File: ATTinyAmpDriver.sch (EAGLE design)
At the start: 34 parts, among them Q1 SI2301CDS, Q2 BC846, U1 SPX5205M5-L-3-3, U2 ATTINY5-TSHR, U3 MCP6L2-X_SN, X2 INPUT

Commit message: Board Complete
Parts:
- removed X2: INPUT, con-phoenix-254:MPT3
- added U$1: CON_TAILLIGHT, Combined:CON_TAILLIGHT
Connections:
- net +14V: now also U$1.L1; no longer X2-1.1
- net GND: now also U$1.H2, U$1.L2; no longer X2-2.1
- net N$1: now also U$1.H1; no longer X2-3.1
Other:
- moved on the sheet: D1, R6, R7
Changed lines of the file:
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@@
 <attribute name="DIGIKEY_COST" value=".60"/>
 </part>
-<part name="X2" library="con-phoenix-254" deviceset="MPT3" device="" value="INPUT"/>
 <part name="SUPPLY1" library="supply2" deviceset="+14V" device=""/>
 <part name="SUPPLY2" library="supply2" deviceset="GND" device=""/>
@@
 <part name="LED4" library="Combined" deviceset="LUXEON_REBEL" device="CREE_XP-E"/>
 <part name="SUPPLY20" library="supply2" deviceset="GND" device=""/>
+<part name="U$1" library="Combined" deviceset="CON_TAILLIGHT" device=""/>
 </parts>
 <sheets>
@@
 <attribute name="DIGIKEY_COST" x="66.04" y="180.34" size="1.778" layer="96" display="off"/>
 </instance>
-<instance part="X2" gate="-1" x="81.28" y="132.08" rot="MR0"/>
-<instance part="X2" gate="-2" x="81.28" y="121.92" rot="MR0"/>
-<instance part="X2" gate="-3" x="81.28" y="127" rot="MR0"/>
-<instance part="SUPPLY1" gate="G$1" x="91.44" y="139.7"/>
-<instance part="SUPPLY2" gate="GND" x="91.44" y="114.3"/>
+<instance part="SUPPLY1" gate="G$1" x="91.44" y="144.78"/>
+<instance part="SUPPLY2" gate="GND" x="91.44" y="109.22"/>
 <instance part="SUPPLY3" gate="G$1" x="96.52" y="195.58"/>
 <instance part="C3" gate="G$1" x="91.44" y="172.72">
@@
 </instance>
 <instance part="SUPPLY9" gate="G$1" x="38.1" y="195.58"/>
-<instance part="R6" gate="G$1" x="106.68" y="127" rot="R180">
-<attribute name="DIGIKEY" x="106.68" y="127" size="1.778" layer="96" rot="R180" display="off"/>
-<attribute name="DIGIKEY_COST" x="106.68" y="127" size="1.778" layer="96" rot="R180" display="off"/>
-</instance>
-<instance part="R7" gate="G$1" x="114.3" y="119.38" rot="R270">
-<attribute name="DIGIKEY" x="114.3" y="119.38" size="1.778" layer="96" rot="R270" display="off"/>
-<attribute name="DIGIKEY_COST" x="114.3" y="119.38" size="1.778" layer="96" rot="R270" display="off"/>
-</instance>
-<instance part="SUPPLY10" gate="GND" x="114.3" y="109.22"/>
+<instance part="R6" gate="G$1" x="106.68" y="132.08" rot="R180">
+<attribute name="DIGIKEY" x="106.68" y="132.08" size="1.778" layer="96" rot="R180" display="off"/>
+<attribute name="DIGIKEY_COST" x="106.68" y="132.08" size="1.778" layer="96" rot="R180" display="off"/>
+</instance>
+<instance part="R7" gate="G$1" x="114.3" y="124.46" rot="R270">
+<attribute name="DIGIKEY" x="114.3" y="124.46" size="1.778" layer="96" rot="R270" display="off"/>
+<attribute name="DIGIKEY_COST" x="114.3" y="124.46" size="1.778" layer="96" rot="R270" display="off"/>
+</instance>
+<instance part="SUPPLY10" gate="GND" x="114.3" y="114.3"/>
 <instance part="R2" gate="G$1" x="58.42" y="73.66" rot="MR270">
 <attribute name="DIGIKEY" x="58.42" y="73.66" size="1.778" layer="96" rot="MR270" display="off"/>
@@
 </instance>
 <instance part="SUPPLY22" gate="GND" x="243.84" y="35.56"/>
-<instance part="D1" gate="G$1" x="93.98" y="127" smashed="yes">
-<attribute name="DIGIKEY" x="93.98" y="127" size="1.778" layer="96" display="off"/>
-<attribute name="DIGIKEY_COST" x="93.98" y="127" size="1.778" layer="96" display="off"/>
-<attribute name="NAME" x="96.52" y="127.4826" size="1.778" layer="95"/>
+<instance part="D1" gate="G$1" x="93.98" y="132.08" smashed="yes">
+<attribute name="DIGIKEY" x="93.98" y="132.08" size="1.778" layer="96" display="off"/>
+<attribute name="DIGIKEY_COST" x="93.98" y="132.08" size="1.778" layer="96" display="off"/>
+<attribute name="NAME" x="96.52" y="132.5626" size="1.778" layer="95"/>
 </instance>
 <instance part="R8" gate="G$1" x="228.6" y="124.46" rot="MR270">
@@
 <instance part="LED4" gate="TH" x="149.86" y="30.48" rot="R180"/>
 <instance part="SUPPLY20" gate="GND" x="134.62" y="15.24"/>
+<instance part="U$1" gate="G$1" x="83.82" y="127"/>
 </instances>
 <busses>
@@
 <segment>
 <pinref part="SUPPLY2" gate="GND" pin="GND"/>
+<wire x1="91.44" y1="116.84" x2="91.44" y2="111.76" width="0.1524" layer="91"/>
+<wire x1="83.82" y1="116.84" x2="91.44" y2="116.84" width="0.1524" layer="91"/>
+<pinref part="U$1" gate="G$1" pin="L2"/>
+<pinref part="U$1" gate="G$1" pin="H2"/>
+<wire x1="83.82" y1="121.92" x2="91.44" y2="121.92" width="0.1524" layer="91"/>
 <wire x1="91.44" y1="121.92" x2="91.44" y2="116.84" width="0.1524" layer="91"/>
-<pinref part="X2" gate="-2" pin="1"/>
-<wire x1="83.82" y1="121.92" x2="91.44" y2="121.92" width="0.1524" layer="91"/>
+<junction x="91.44" y="116.84"/>
 </segment>
 <segment>
@@
 <pinref part="R7" gate="G$1" pin="2"/>
 <pinref part="SUPPLY10" gate="GND" pin="GND"/>
-<wire x1="114.3" y1="114.3" x2="114.3" y2="111.76" width="0.1524" layer="91"/>
+<wire x1="114.3" y1="119.38" x2="114.3" y2="116.84" width="0.1524" layer="91"/>
 </segment>
 <segment>
@@
 <net name="+14V" class="0">
 <segment>
-<pinref part="X2" gate="-1" pin="1"/>
 <pinref part="SUPPLY1" gate="G$1" pin="+14V"/>
-<wire x1="83.82" y1="132.08" x2="91.44" y2="132.08" width="0.1524" layer="91"/>
-<wire x1="91.44" y1="132.08" x2="91.44" y2="137.16" width="0.1524" layer="91"/>
+<wire x1="83.82" y1="137.16" x2="91.44" y2="137.16" width="0.1524" layer="91"/>
+<wire x1="91.44" y1="137.16" x2="91.44" y2="142.24" width="0.1524" layer="91"/>
+<pinref part="U$1" gate="G$1" pin="L1"/>
 </segment>
 <segment>
@@
 <segment>
 <pinref part="R6" gate="G$1" pin="1"/>
-<wire x1="111.76" y1="127" x2="114.3" y2="127" width="0.1524" layer="91"/>
+<wire x1="111.76" y1="132.08" x2="114.3" y2="132.08" width="0.1524" layer="91"/>
 <pinref part="R7" gate="G$1" pin="1"/>
-<wire x1="114.3" y1="127" x2="121.92" y2="127" width="0.1524" layer="91"/>
-<wire x1="114.3" y1="124.46" x2="114.3" y2="127" width="0.1524" layer="91"/>
-<junction x="114.3" y="127"/>
-<label x="121.92" y="127" size="1.778" layer="95" xref="yes"/>
+<wire x1="114.3" y1="132.08" x2="121.92" y2="132.08" width="0.1524" layer="91"/>
+<wire x1="114.3" y1="129.54" x2="114.3" y2="132.08" width="0.1524" layer="91"/>
+<junction x="114.3" y="132.08"/>
+<label x="121.92" y="132.08" size="1.778" layer="95" xref="yes"/>
 </segment>
 <segment>
@@
 <net name="N$1" class="0">
 <segment>
-<pinref part="X2" gate="-3" pin="1"/>
 <pinref part="D1" gate="G$1" pin="A"/>
-<wire x1="83.82" y1="127" x2="91.44" y2="127" width="0.1524" layer="91"/>
+<wire x1="83.82" y1="132.08" x2="91.44" y2="132.08" width="0.1524" layer="91"/>
+<pinref part="U$1" gate="G$1" pin="H1"/>
 </segment>
 </net>
@@
 <pinref part="D1" gate="G$1" pin="C"/>
 <pinref part="R6" gate="G$1" pin="2"/>
-<wire x1="96.52" y1="127" x2="101.6" y2="127" width="0.1524" layer="91"/>
-</segment>
-</net>
+<wire x1="96.52" y1="132.08" x2="101.6" y2="132.08" width="0.1524" layer="91"/>
+</segment>
+</net>

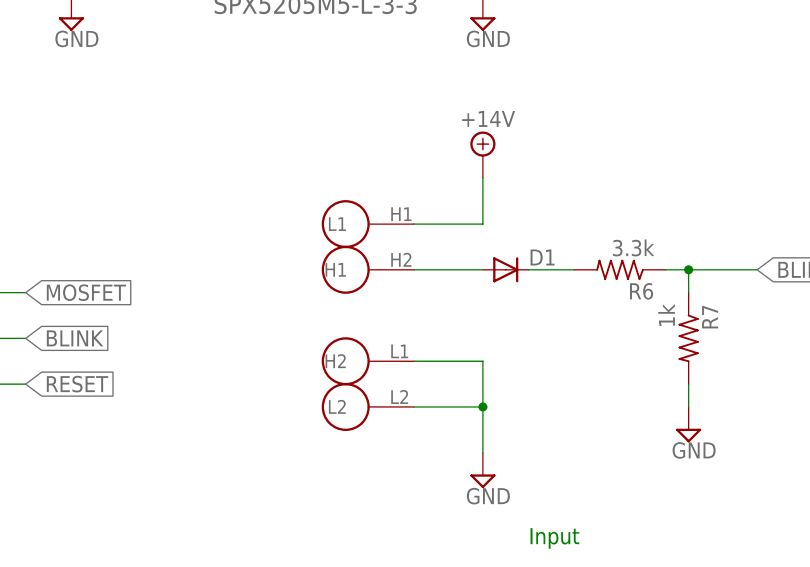
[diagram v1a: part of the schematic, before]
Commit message: Fixed pin polarity on Tail Connecter
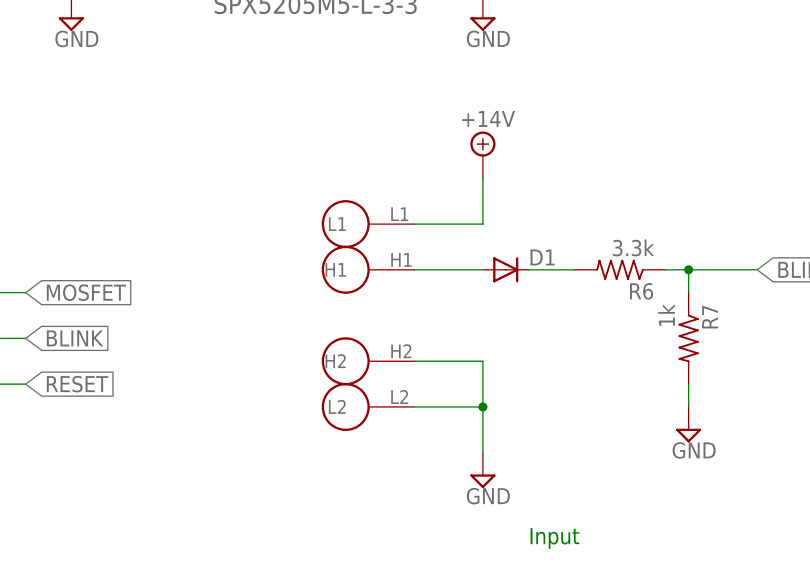
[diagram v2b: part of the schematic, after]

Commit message: Created programming fixture
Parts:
- +5V, GND, MEASURE, OUTA, PWM, RESET, TPICLK, TPIDATA: device Personal:TPI -> Combined:TPI
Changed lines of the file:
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@@
 <layer number="97" name="Info" color="7" fill="1" visible="yes" active="yes"/>
 <layer number="98" name="Guide" color="6" fill="1" visible="yes" active="yes"/>
+<layer number="100" name="TestPads" color="7" fill="1" visible="yes" active="yes"/>
 <layer number="250" name="Descript" color="3" fill="1" visible="no" active="no"/>
 <layer number="251" name="SMDround" color="12" fill="11" visible="no" active="no"/>
@@
 <attribute name="DIGIKEY_COST" value=".04"/>
 </part>
-<part name="TPIDATA" library="Personal" deviceset="TPI" device=""/>
-<part name="TPICLK" library="Personal" deviceset="TPI" device=""/>
-<part name="+5V" library="Personal" deviceset="TPI" device=""/>
-<part name="GND" library="Personal" deviceset="TPI" device=""/>
+<part name="TPIDATA" library="Combined" deviceset="TPI" device=""/>
+<part name="TPICLK" library="Combined" deviceset="TPI" device=""/>
+<part name="+5V" library="Combined" deviceset="TPI" device=""/>
+<part name="GND" library="Combined" deviceset="TPI" device=""/>
 <part name="SUPPLY15" library="supply2" deviceset="VCC" device=""/>
 <part name="SUPPLY16" library="supply2" deviceset="GND" device=""/>
@@
 </part>
 <part name="SUPPLY17" library="supply2" deviceset="GND" device=""/>
-<part name="RESET" library="Personal" deviceset="TPI" device=""/>
+<part name="RESET" library="Combined" deviceset="TPI" device=""/>
 <part name="SUPPLY19" library="supply2" deviceset="GND" device=""/>
 <part name="SUPPLY21" library="supply2" deviceset="VCC" device=""/>
@@
 <attribute name="DIGIKEY_COST" value=".04"/>
 </part>
-<part name="PWM" library="Personal" deviceset="TPI" device=""/>
-<part name="MEASURE" library="Personal" deviceset="TPI" device=""/>
-<part name="OUTA" library="Personal" deviceset="TPI" device=""/>
+<part name="PWM" library="Combined" deviceset="TPI" device=""/>
+<part name="MEASURE" library="Combined" deviceset="TPI" device=""/>
+<part name="OUTA" library="Combined" deviceset="TPI" device=""/>
 <part name="LED1" library="Combined" deviceset="LUXEON_REBEL" device="CREE_XP-E"/>
 <part name="LED2" library="Combined" deviceset="LUXEON_REBEL" device="CREE_XP-E"/>
